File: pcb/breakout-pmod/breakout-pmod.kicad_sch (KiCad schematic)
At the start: 13 parts, among them J1 FX18-120P-0.8SV20

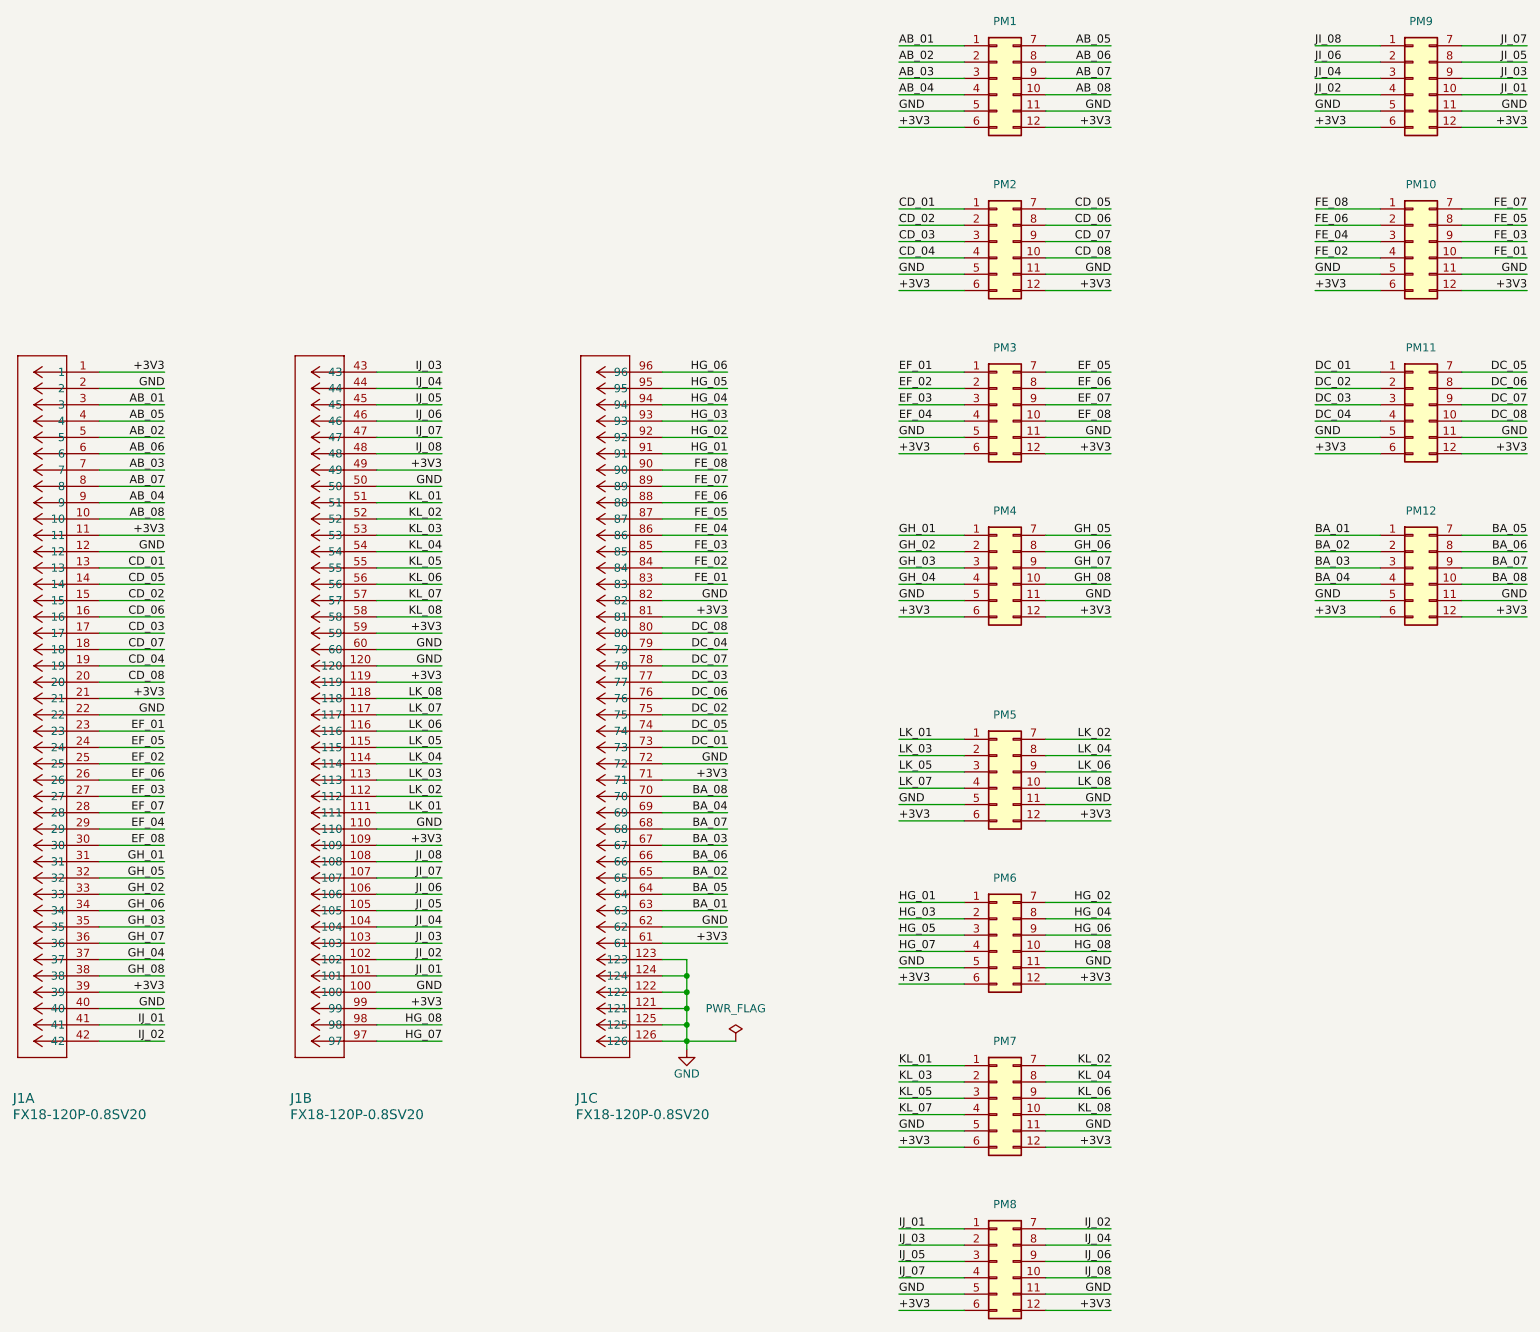
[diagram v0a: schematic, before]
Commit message: [pmod] fix order of IJ pmod
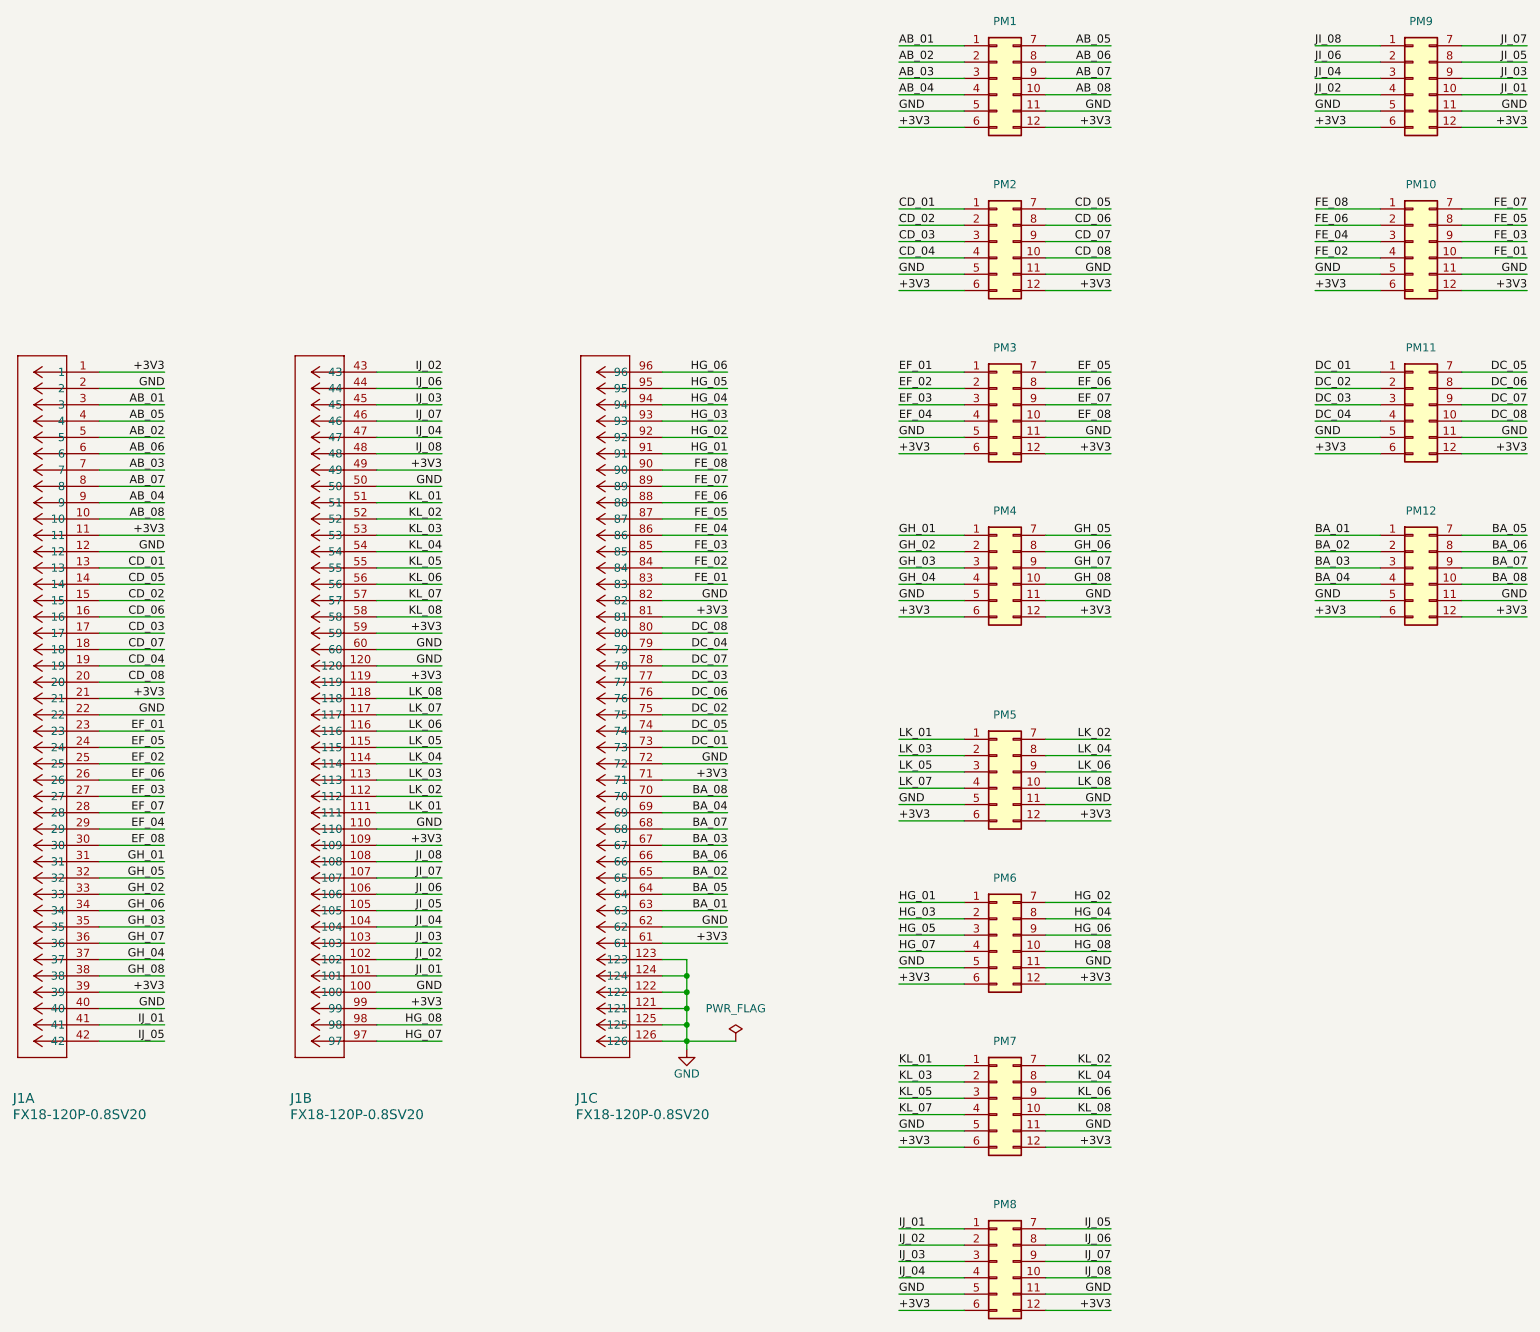
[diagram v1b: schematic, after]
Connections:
- net IJ_02: now also J1.43, PM8.2 (Pin_2); no longer J1.42, PM8.7 (Pin_7)
- net IJ_03: now also J1.45, PM8.3 (Pin_3); no longer J1.43, PM8.2 (Pin_2)
- net IJ_04: now also J1.47, PM8.4 (Pin_4); no longer J1.44, PM8.8 (Pin_8)
- net IJ_05: now also J1.42, PM8.7 (Pin_7); no longer J1.45, PM8.3 (Pin_3)
- net IJ_06: now also J1.44, PM8.8 (Pin_8); no longer J1.46, PM8.9 (Pin_9)
- net IJ_07: now also J1.46, PM8.9 (Pin_9); no longer J1.47, PM8.4 (Pin_4)
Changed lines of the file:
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@@
 	)
 	(label "IJ_02"
-		(at 198.12 223.52 180)
-		(fields_autoplaced yes)
-		(effects
-			(font
-				(size 1.27 1.27)
-			)
-			(justify right bottom)
+		(at 165.1 226.06 0)
+		(fields_autoplaced yes)
+		(effects
+			(font
+				(size 1.27 1.27)
+			)
+			(justify left bottom)
 		)
 	)
@@
 	)
 	(label "IJ_04"
-		(at 93.98 92.71 180)
+		(at 93.98 100.33 180)
 		(fields_autoplaced yes)
 		(effects
@@
 	)
 	(label "IJ_06"
-		(at 198.12 228.6 180)
+		(at 198.12 226.06 180)
 		(fields_autoplaced yes)
 		(effects
@@
 	)
 	(label "IJ_05"
-		(at 93.98 95.25 180)
+		(at 50.8 194.31 180)
 		(fields_autoplaced yes)
 		(effects
@@
 	)
 	(label "IJ_06"
-		(at 93.98 97.79 180)
+		(at 93.98 92.71 180)
 		(fields_autoplaced yes)
 		(effects
@@
 	)
 	(label "IJ_07"
-		(at 93.98 100.33 180)
+		(at 93.98 97.79 180)
 		(fields_autoplaced yes)
 		(effects
@@
 	)
 	(label "IJ_03"
-		(at 165.1 226.06 0)
+		(at 165.1 228.6 0)
 		(fields_autoplaced yes)
 		(effects
@@
 	)
 	(label "IJ_07"
-		(at 165.1 231.14 0)
-		(fields_autoplaced yes)
-		(effects
-			(font
-				(size 1.27 1.27)
-			)
-			(justify left bottom)
+		(at 198.12 228.6 180)
+		(fields_autoplaced yes)
+		(effects
+			(font
+				(size 1.27 1.27)
+			)
+			(justify right bottom)
 		)
 	)
@@
 	)
 	(label "IJ_05"
-		(at 165.1 228.6 0)
-		(fields_autoplaced yes)
-		(effects
-			(font
-				(size 1.27 1.27)
-			)
-			(justify left bottom)
+		(at 198.12 223.52 180)
+		(fields_autoplaced yes)
+		(effects
+			(font
+				(size 1.27 1.27)
+			)
+			(justify right bottom)
 		)
 	)
@@
 	)
 	(label "IJ_04"
-		(at 198.12 226.06 180)
-		(fields_autoplaced yes)
-		(effects
-			(font
-				(size 1.27 1.27)
-			)
-			(justify right bottom)
+		(at 165.1 231.14 0)
+		(fields_autoplaced yes)
+		(effects
+			(font
+				(size 1.27 1.27)
+			)
+			(justify left bottom)
 		)
 	)
@@
 	)
 	(label "IJ_03"
-		(at 93.98 90.17 180)
+		(at 93.98 95.25 180)
 		(fields_autoplaced yes)
 		(effects
@@
 	)
 	(label "IJ_02"
-		(at 50.8 194.31 180)
-		(fields_autoplaced yes)
-		(effects
+		(at 93.98 90.17 180)
+		(fields_autoplaced yes)
+		(effects

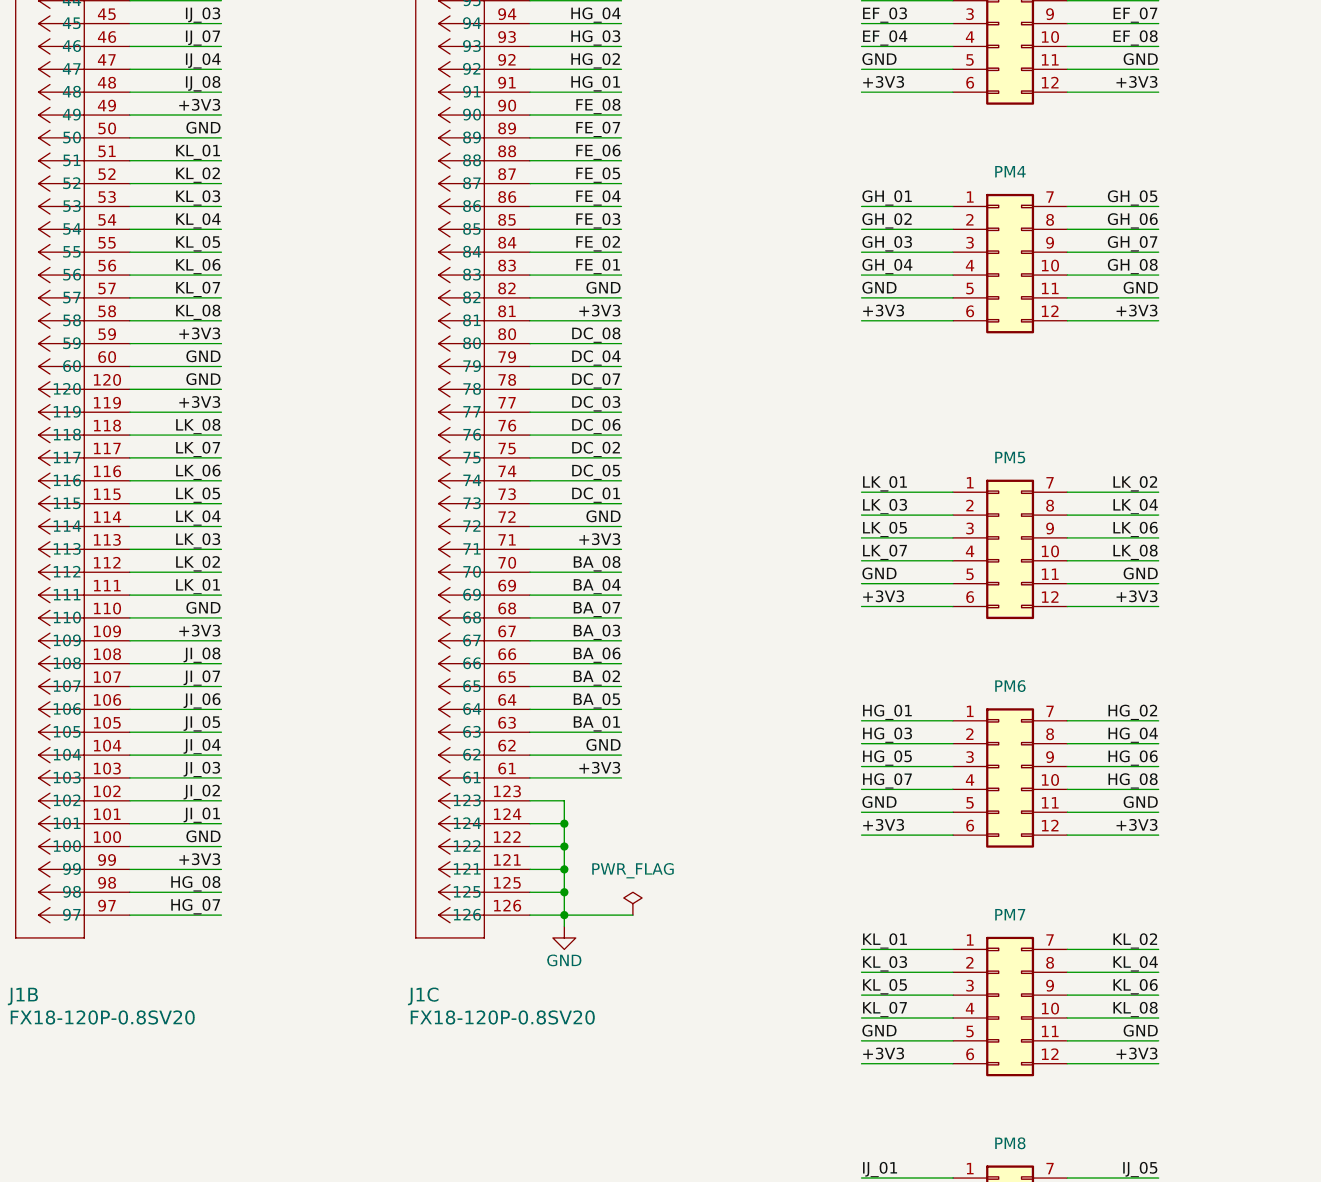
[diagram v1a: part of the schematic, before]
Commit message: [pmod] fix order of KL pmod
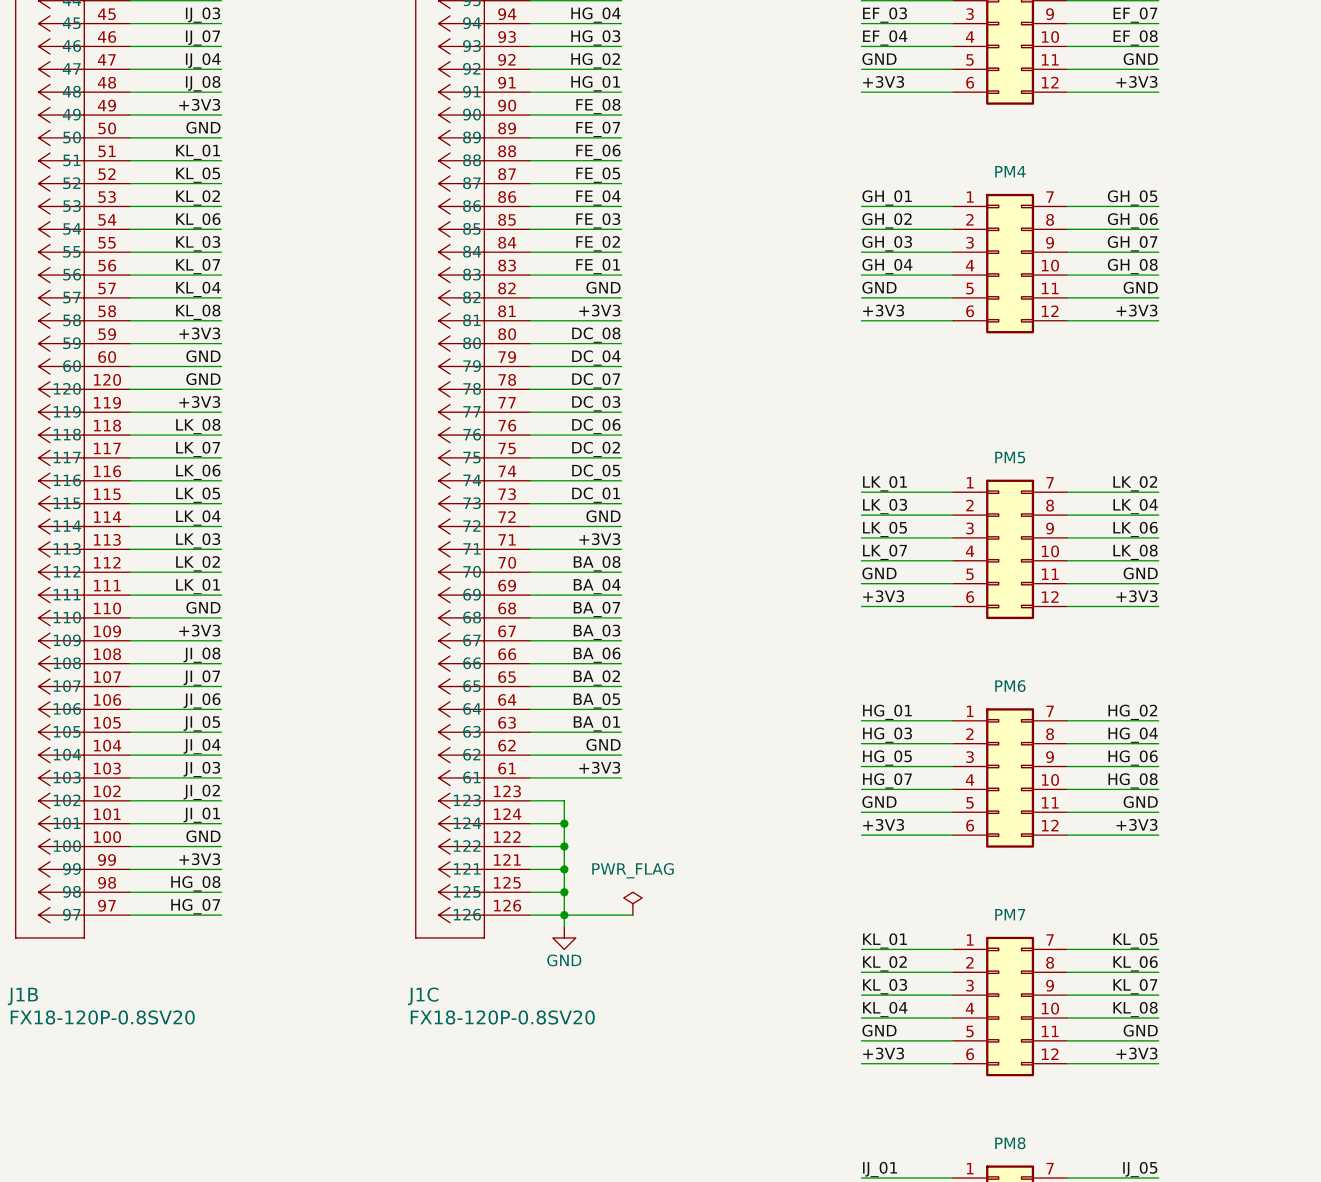
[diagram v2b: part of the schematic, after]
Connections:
- net KL_02: now also J1.53, PM7.2 (Pin_2); no longer J1.52, PM7.7 (Pin_7)
- net KL_03: now also J1.55, PM7.3 (Pin_3); no longer J1.53, PM7.2 (Pin_2)
- net KL_04: now also J1.57, PM7.4 (Pin_4); no longer J1.54, PM7.8 (Pin_8)
- net KL_05: now also J1.52, PM7.7 (Pin_7); no longer J1.55, PM7.3 (Pin_3)
- net KL_06: now also J1.54, PM7.8 (Pin_8); no longer J1.56, PM7.9 (Pin_9)
- net KL_07: now also J1.56, PM7.9 (Pin_9); no longer J1.57, PM7.4 (Pin_4)
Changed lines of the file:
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@@
 	)
 	(label "KL_06"
-		(at 93.98 123.19 180)
+		(at 93.98 118.11 180)
 		(fields_autoplaced yes)
 		(effects
@@
 	)
 	(label "KL_05"
-		(at 93.98 120.65 180)
+		(at 93.98 113.03 180)
 		(fields_autoplaced yes)
 		(effects
@@
 	)
 	(label "KL_05"
-		(at 165.1 203.2 0)
-		(fields_autoplaced yes)
-		(effects
-			(font
-				(size 1.27 1.27)
-			)
-			(justify left bottom)
+		(at 198.12 198.12 180)
+		(fields_autoplaced yes)
+		(effects
+			(font
+				(size 1.27 1.27)
+			)
+			(justify right bottom)
 		)
 	)
@@
 	)
 	(label "KL_03"
-		(at 93.98 115.57 180)
+		(at 93.98 120.65 180)
 		(fields_autoplaced yes)
 		(effects
@@
 	)
 	(label "KL_07"
-		(at 165.1 205.74 0)
-		(fields_autoplaced yes)
-		(effects
-			(font
-				(size 1.27 1.27)
-			)
-			(justify left bottom)
+		(at 198.12 203.2 180)
+		(fields_autoplaced yes)
+		(effects
+			(font
+				(size 1.27 1.27)
+			)
+			(justify right bottom)
 		)
 	)
@@
 	)
 	(label "KL_02"
-		(at 198.12 198.12 180)
-		(fields_autoplaced yes)
-		(effects
-			(font
-				(size 1.27 1.27)
-			)
-			(justify right bottom)
+		(at 165.1 200.66 0)
+		(fields_autoplaced yes)
+		(effects
+			(font
+				(size 1.27 1.27)
+			)
+			(justify left bottom)
 		)
 	)
@@
 	)
 	(label "KL_06"
-		(at 198.12 203.2 180)
+		(at 198.12 200.66 180)
 		(fields_autoplaced yes)
 		(effects
@@
 	)
 	(label "KL_04"
-		(at 93.98 118.11 180)
+		(at 93.98 125.73 180)
 		(fields_autoplaced yes)
 		(effects
@@
 	)
 	(label "KL_04"
-		(at 198.12 200.66 180)
-		(fields_autoplaced yes)
-		(effects
-			(font
-				(size 1.27 1.27)
-			)
-			(justify right bottom)
+		(at 165.1 205.74 0)
+		(fields_autoplaced yes)
+		(effects
+			(font
+				(size 1.27 1.27)
+			)
+			(justify left bottom)
 		)
 	)
@@
 	)
 	(label "KL_07"
-		(at 93.98 125.73 180)
+		(at 93.98 123.19 180)
 		(fields_autoplaced yes)
 		(effects
@@
 	)
 	(label "KL_03"
-		(at 165.1 200.66 0)
+		(at 165.1 203.2 0)
 		(fields_autoplaced yes)
 		(effects
@@
 	)
 	(label "KL_02"
-		(at 93.98 113.03 180)
-		(fields_autoplaced yes)
-		(effects
+		(at 93.98 115.57 180)
+		(fields_autoplaced yes)
+		(effects
